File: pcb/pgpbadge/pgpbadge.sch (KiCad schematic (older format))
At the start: 0 parts

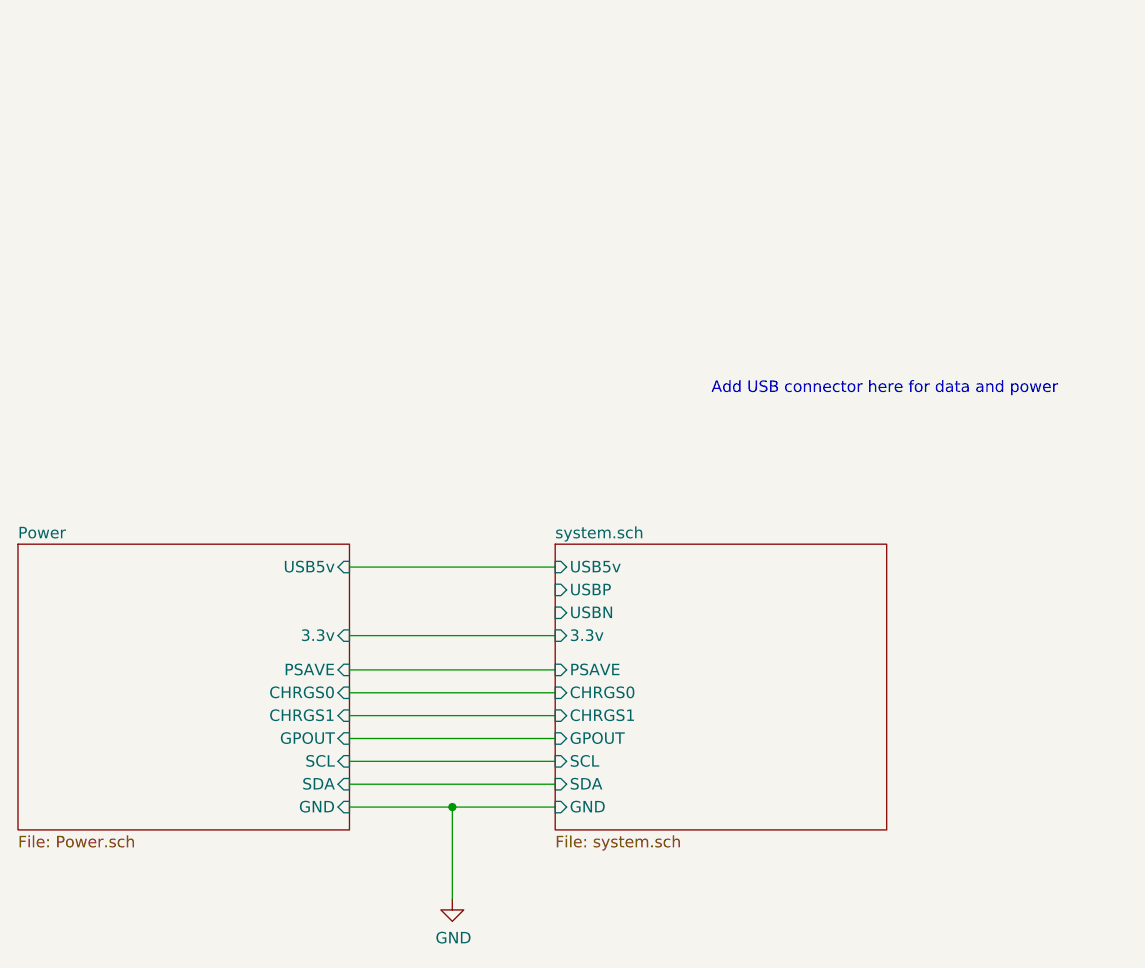
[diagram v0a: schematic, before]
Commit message: Board layout and routing done, need to fix DRC's, add more ground stitching, clean up silscreen, and review
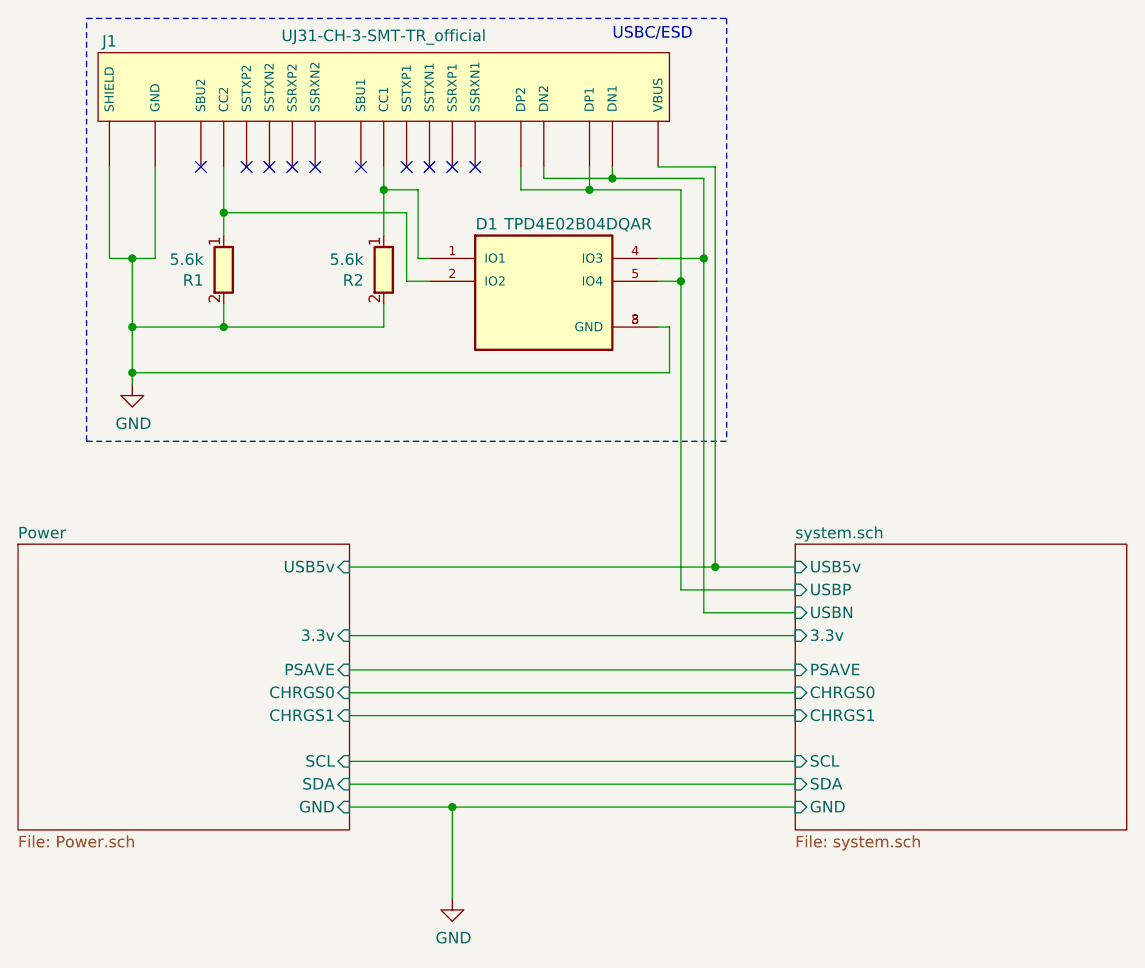
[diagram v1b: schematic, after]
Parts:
- added D1: TPD4E02B04DQAR, pgpbadge:DIO_TPD4E02B04DQAR, symbol pgpbadge:TPD4E02B04DQAR
- added J1: UJ31-CH-3-SMT-TR_official, CUI_UJ31-CH-3-SMT-TR, symbol pgpbadge:UJ31-CH-3-SMT-TR_official
- added R1, R2: 5.6k, Resistor_SMD:R_0402_1005Metric, symbol pgpbadge:R
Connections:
- net GND: now also D1.3 (GND), D1.8 (GND), J1.0 (SHIELD), J1.A1 (GND), J1.A12 (GND), J1.B1 (GND), J1.B12 (GND), R1.2, R2.2
- net Power/USB5v: now also J1.A4 (VBUS), J1.A9 (VBUS), J1.B4 (VBUS), J1.B9 (VBUS)
- net system.sch/USBN: now also D1.4 (IO3), J1.A7 (DN1), J1.B7 (DN2)
- net system.sch/USBP: now also D1.5 (IO4), J1.A6 (DP1), J1.B6 (DP2)
- new net: D1.1 (IO1), J1.A5 (CC1), R2.1
- new net: D1.2 (IO2), J1.B5 (CC2), R1.1
- no-connect marks 0 -> 10
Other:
- note added: "USBC/ESD"
- note removed: "Add USB connector here for data and power"
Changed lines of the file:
@@
 F5 "GND" I R 5000 4550 50
 F6 "USB5v" I R 5000 3500 50
-F7 "GPOUT" I R 5000 4250 50
-F8 "CHRGS0" I R 5000 4050 50
-F9 "CHRGS1" I R 5000 4150 50
-F10 "PSAVE" I R 5000 3950 50
+F7 "CHRGS0" I R 5000 4050 50
+F8 "CHRGS1" I R 5000 4150 50
+F9 "PSAVE" I R 5000 3950 50
 $EndSheet
 $Comp
@@
 Connection ~ 5450 4550
 Wire Wire Line
-	5450 4550 5900 4550
+	5450 4550 6950 4550
 $Sheet
-S 5900 3400 1450 1250
+S 6950 3400 1450 1250
 U 5E76E48F
 F0 "system.sch" 50
 F1 "system.sch" 50
-F2 "3.3v" I L 5900 3800 50
-F3 "GND" I L 5900 4550 50
-F4 "SCL" I L 5900 4350 50
-F5 "SDA" I L 5900 4450 50
-F6 "USB5v" I L 5900 3500 50
-F7 "USBP" I L 5900 3600 50
-F8 "USBN" I L 5900 3700 50
-F9 "GPOUT" I L 5900 4250 50
-F10 "CHRGS0" I L 5900 4050 50
-F11 "CHRGS1" I L 5900 4150 50
-F12 "PSAVE" I L 5900 3950 50
+F2 "3.3v" I L 6950 3800 50
+F3 "GND" I L 6950 4550 50
+F4 "SCL" I L 6950 4350 50
+F5 "SDA" I L 6950 4450 50
+F6 "USB5v" I L 6950 3500 50
+F7 "USBP" I L 6950 3600 50
+F8 "USBN" I L 6950 3700 50
+F9 "CHRGS0" I L 6950 4050 50
+F10 "CHRGS1" I L 6950 4150 50
+F11 "PSAVE" I L 6950 3950 50
 $EndSheet
 Wire Wire Line
-	5000 3800 5900 3800
-Wire Wire Line
-	5000 3950 5900 3950
-Wire Wire Line
-	5900 4050 5000 4050
-Wire Wire Line
-	5000 4150 5900 4150
-Wire Wire Line
-	5900 4250 5000 4250
-Wire Wire Line
-	5000 4350 5900 4350
-Wire Wire Line
-	5900 4450 5000 4450
-Wire Wire Line
-	5900 3500 5000 3500
-Text Notes 8100 2750 2    50   ~ 0
-Add USB connector here for data and power
+	5000 3800 6950 3800
+Wire Wire Line
+	5000 3950 6950 3950
+Wire Wire Line
+	6950 4050 5000 4050
+Wire Wire Line
+	5000 4150 6950 4150
+Wire Wire Line
+	5000 4350 6950 4350
+Wire Wire Line
+	6950 4450 5000 4450
+$Comp
+L power:GND #PWR01
+U 1 1 5EB197BF
+P 4050 2700
+F 0 "#PWR01" H 4050 2450 50  0001 C CNN
+F 1 "GND" H 4055 2527 50  0000 C CNN
+F 2 "" H 4050 2700 50  0001 C CNN
+F 3 "" H 4050 2700 50  0001 C CNN
+	1    4050 2700
+	1    0    0    -1
+$EndComp
+Wire Wire Line
+	3950 2150 4050 2150
+Wire Wire Line
+	4050 2150 4050 2450
+Wire Wire Line
+	4150 2150 4050 2150
+Connection ~ 4050 2150
+NoConn ~ 5550 1750
+NoConn ~ 5450 1750
+NoConn ~ 5350 1750
+NoConn ~ 5250 1750
+NoConn ~ 5050 1750
+NoConn ~ 4850 1750
+NoConn ~ 4750 1750
+NoConn ~ 4650 1750
+NoConn ~ 4550 1750
+NoConn ~ 4350 1750
+$Comp
+L pgpbadge:UJ31-CH-3-SMT-TR_official J1
+U 1 1 5EB151FF
+P 5150 1250
+F 0 "J1" V 5100 50  50  0000 C CNN
+F 1 "UJ31-CH-3-SMT-TR_official" V 5076 1250 50  0000 C CNN
+F 2 "CUI_UJ31-CH-3-SMT-TR" H 6200 1000 50  0001 L BNN
+F 3 "https://www.cuidevices.com/product/resource/uj31-ch-3-smt-tr.pdf" H 5150 1250 50  0001 L BNN
+F 4 "102-4484-1-ND" H 6500 1100 50  0001 L BNN "DPN"
+F 5 "UJ31-CH-3-SMT-TR" H 6300 1200 50  0001 L BNN "PN"
+F 6 "https://www.digikey.com/product-detail/en/cui-devices/UJ31-CH-3-SMT-TR/102-4484-1-ND/8024064" V 4900 1250 50  0001 C CNN "URL"
+	1    5150 1250
+	0    1    1    0
+$EndComp
+$Comp
+L pgpbadge:R R?
+U 1 1 5EB1F8E4
+P 5150 2200
+AR Path="/5E76E48F/5EB1F8E4" Ref="R?"  Part="1"
+AR Path="/5E76D91B/5EB1F8E4" Ref="R?"  Part="1"
+AR Path="/5EB1F8E4" Ref="R2"  Part="1"
+F 0 "R2" H 5062 2154 50  0000 R CNN
+F 1 "5.6k" H 5062 2245 50  0000 R CNN
+F 2 "Resistor_SMD:R_0402_1005Metric" H 5150 2200 50  0001 C CNN
+F 3 "https://b2b-api.panasonic.eu/file_stream/pids/fileversion/1242" H 5150 2200 50  0001 C CNN
+F 4 "P5.6KJCT-ND" H 5150 2200 50  0001 C CNN "DPN"
+F 5 "ERJ-2GEJ562X" H 5150 2200 50  0001 C CNN "PN"
+F 6 "https://www.digikey.com/product-detail/en/panasonic-electronic-components/ERJ-2GEJ562X/P5-6KJCT-ND/147045" H 5150 2200 50  0001 C CNN "URL"
+	1    5150 2200
+	1    0    0    -1
+$EndComp
+$Comp
+L pgpbadge:R R?
+U 1 1 5EB1FAB4
+P 4450 2200
+AR Path="/5E76E48F/5EB1FAB4" Ref="R?"  Part="1"
+AR Path="/5E76D91B/5EB1FAB4" Ref="R?"  Part="1"
+AR Path="/5EB1FAB4" Ref="R1"  Part="1"
+F 0 "R1" H 4362 2154 50  0000 R CNN
+F 1 "5.6k" H 4362 2245 50  0000 R CNN
+F 2 "Resistor_SMD:R_0402_1005Metric" H 4450 2200 50  0001 C CNN
+F 3 "https://b2b-api.panasonic.eu/file_stream/pids/fileversion/1242" H 4450 2200 50  0001 C CNN
+F 4 "P5.6KJCT-ND" H 4450 2200 50  0001 C CNN "DPN"
+F 5 "ERJ-2GEJ562X" H 4450 2200 50  0001 C CNN "PN"
+F 6 "https://www.digikey.com/product-detail/en/panasonic-electronic-components/ERJ-2GEJ562X/P5-6KJCT-ND/147045" H 4450 2200 50  0001 C CNN "URL"
+	1    4450 2200
+	1    0    0    -1
+$EndComp
+Wire Wire Line
+	4450 2350 4450 2450
+Wire Wire Line
+	4450 2450 4050 2450
+Connection ~ 4050 2450
+Wire Wire Line
+	4050 2450 4050 2650
+Wire Wire Line
+	5150 2350 5150 2450
+Wire Wire Line
+	5150 2450 4450 2450
+Connection ~ 4450 2450
+$Comp
+L pgpbadge:TPD4E02B04DQAR D1
+U 1 1 5EB22D88
+P 5850 2350
+F 0 "D1" H 5600 2700 50  0000 C CNN
+F 1 "TPD4E02B04DQAR" H 6000 2700 50  0000 C CNN
+F 2 "pgpbadge:DIO_TPD4E02B04DQAR" H 5450 1950 50  0001 L BNN
+F 3 "July 2016" H 5650 1550 50  0001 L BNN
+F 4 "296-43875-1-ND" H 5500 1850 50  0001 L BNN "DPN"
+F 5 "TPD4E02B04DQAR" H 5450 1750 50  0001 L BNN "PN"
+F 6 "https://www.digikey.com/product-detail/en/texas-instruments/TPD4E02B04DQAR/296-43875-1-ND/5880543" H 5850 1700 50  0001 C CNN "URL"
+	1    5850 2350
+	1    0    0    -1
+$EndComp
+Wire Wire Line
+	4150 1750 4150 2150
+Wire Wire Line
+	3950 1750 3950 2150
+Wire Wire Line
+	6350 2450 6400 2450
+Wire Wire Line
+	6400 2450 6400 2650
+Wire Wire Line
+	6400 2650 4050 2650
+Connection ~ 4050 2650
+Wire Wire Line
+	4050 2650 4050 2700
+Wire Wire Line
+	5150 2050 5150 1850
+Wire Wire Line
+	4450 2050 4450 1950
+Wire Wire Line
+	5350 2150 5300 2150
+Wire Wire Line
+	5300 2150 5300 1850
+Wire Wire Line
+	5300 1850 5150 1850
+Connection ~ 5150 1850
+Wire Wire Line
+	5150 1850 5150 1750
+Wire Wire Line
+	5350 2250 5250 2250
+Wire Wire Line
+	5250 2250 5250 1950
+Wire Wire Line
+	5250 1950 4450 1950
+Connection ~ 4450 1950
+Wire Wire Line
+	4450 1950 4450 1750
+Wire Wire Line
+	5850 1750 5850 1800
+Wire Wire Line
+	5850 1800 6150 1800
+Wire Wire Line
+	6150 1800 6150 1750
+Wire Wire Line
+	5750 1750 5750 1850
+Wire Wire Line
+	5750 1850 6050 1850
+Wire Wire Line
+	6050 1850 6050 1750
+Wire Wire Line
+	6350 2150 6550 2150
+Wire Wire Line
+	6550 2150 6550 1800
+Wire Wire Line
+	6550 1800 6150 1800
+Connection ~ 6150 1800
+Wire Wire Line
+	6350 2250 6450 2250
+Wire Wire Line
+	6450 2250 6450 1850
+Wire Wire Line
+	6450 1850 6050 1850
+Connection ~ 6050 1850
+Wire Wire Line
+	6950 3500 6600 3500
+Wire Notes Line
+	6650 1100 6650 2950
+Wire Notes Line
+	3850 2950 3850 1100
+Text Notes 6150 1200 0    50   ~ 0
+USBC/ESD
+Wire Notes Line
+	3850 1100 6650 1100
+Wire Notes Line
+	3850 2950 6650 2950
+Wire Wire Line
+	6350 1750 6600 1750
+Wire Wire Line
+	6600 1750 6600 3500
+Connection ~ 6600 3500
+Wire Wire Line
+	6600 3500 5000 3500
+Wire Wire Line
+	6950 3600 6450 3600
+Wire Wire Line
+	6450 3600 6450 2250
+Connection ~ 6450 2250
+Wire Wire Line
+	6950 3700 6550 3700
+Wire Wire Line
+	6550 3700 6550 2150
+Connection ~ 6550 2150
 $EndSCHEMATC

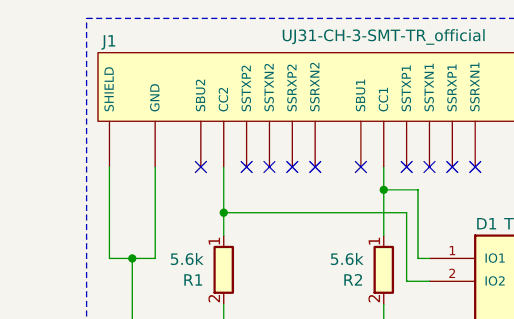
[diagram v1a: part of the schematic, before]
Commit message: DRC's clean, silscreen updated, 1ks changed to 5.6k
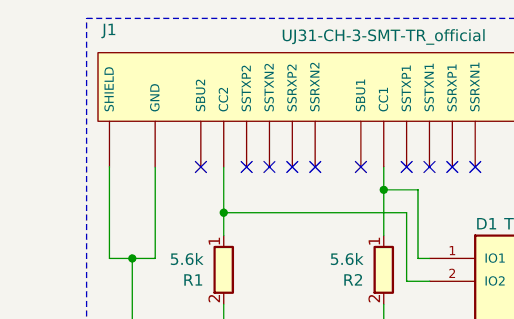
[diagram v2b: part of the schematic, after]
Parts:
- J1: footprint CUI_UJ31-CH-3-SMT-TR -> pgpbadge:CUI_UJ31-CH-3-SMT-TR
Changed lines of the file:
@@
 NoConn ~ 4350 1750
-$Comp
-L pgpbadge:UJ31-CH-3-SMT-TR_official J1
-U 1 1 5EB151FF
-P 5150 1250
-F 0 "J1" V 5100 50  50  0000 C CNN
-F 1 "UJ31-CH-3-SMT-TR_official" V 5076 1250 50  0000 C CNN
-F 2 "CUI_UJ31-CH-3-SMT-TR" H 6200 1000 50  0001 L BNN
-F 3 "https://www.cuidevices.com/product/resource/uj31-ch-3-smt-tr.pdf" H 5150 1250 50  0001 L BNN
-F 4 "102-4484-1-ND" H 6500 1100 50  0001 L BNN "DPN"
-F 5 "UJ31-CH-3-SMT-TR" H 6300 1200 50  0001 L BNN "PN"
-F 6 "https://www.digikey.com/product-detail/en/cui-devices/UJ31-CH-3-SMT-TR/102-4484-1-ND/8024064" V 4900 1250 50  0001 C CNN "URL"
-	1    5150 1250
-	0    1    1    0
-$EndComp
 $Comp
 L pgpbadge:R R?
@@
 	6550 3700 6550 2150
 Connection ~ 6550 2150
+$Comp
+L pgpbadge:UJ31-CH-3-SMT-TR_official J1
+U 1 1 5EB64BEA
+P 5150 1250
+F 0 "J1" V 5050 50  50  0000 C CNN
+F 1 "UJ31-CH-3-SMT-TR_official" V 5076 1250 50  0000 C CNN
+F 2 "pgpbadge:CUI_UJ31-CH-3-SMT-TR" H 6200 1000 50  0001 L BNN
+F 3 "https://www.cuidevices.com/product/resource/uj31-ch-3-smt-tr.pdf" H 5150 1250 50  0001 L BNN
+F 4 "102-4484-1-ND" H 6500 1100 50  0001 L BNN "DPN"
+F 5 "UJ31-CH-3-SMT-TR" H 6300 1200 50  0001 L BNN "PN"
+F 6 "https://www.digikey.com/product-detail/en/cui-devices/UJ31-CH-3-SMT-TR/102-4484-1-ND/8024064" V 4900 1250 50  0001 C CNN "URL"
+	1    5150 1250
+	0    1    1    0
+$EndComp
 $EndSCHEMATC
